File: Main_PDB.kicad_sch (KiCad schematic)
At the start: 126 parts, among them J1 Conn_01x02_MountingPin, J10 Conn_01x04_MountingPin, J11 Conn_01x08, J12 Conn_01x02_MountingPin, J2 Conn_01x02_MountingPin, J3 Conn_01x02_MountingPin, J4 Conn_01x02_MountingPin, J5 Conn_01x02_MountingPin, J6 Conn_01x01_MountingPin, J7 Conn_01x01_MountingPin, J8 Conn_01x02_MountingPin, Q1 PMOS, Q10 NMOS, Q11 NMOS, Q12 NMOS, Q13 NMOS, Q14 NMOS, Q15 NMOS, Q2 NPN, Q5 NMOS, Q7 NMOS, Q8 NMOS, Q9 NMOS, U1 LRM36015, U10 LM5148RGYR, U11 ACS758LCB-100U-PFF-T, U12 TPS48110AQDGXRQ1, U13 LM5148RGYR, U2 ACS758LCB-100U-PFF-T, U3 UCC27524AQDRQ1, U4 ACS758LCB-100U-PFF-T, U5 ACS758LCB-100U-PFF-T, U6 ACS758LCB-100U-PFF-T, U7 LTC4359HDCBPBF, U8 UCC27524AQDRQ1, U9 ACS758LCB-100U-PFF-T

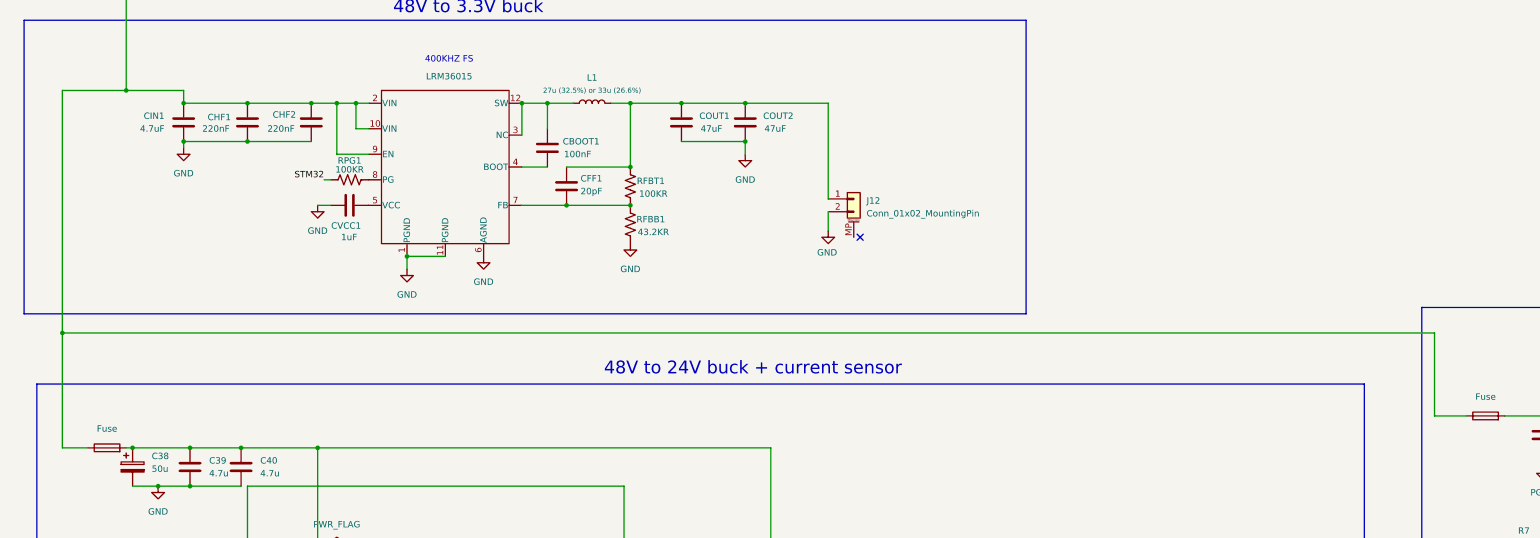
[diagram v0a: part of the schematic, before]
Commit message: Fixed 48V -> 6V buck power source
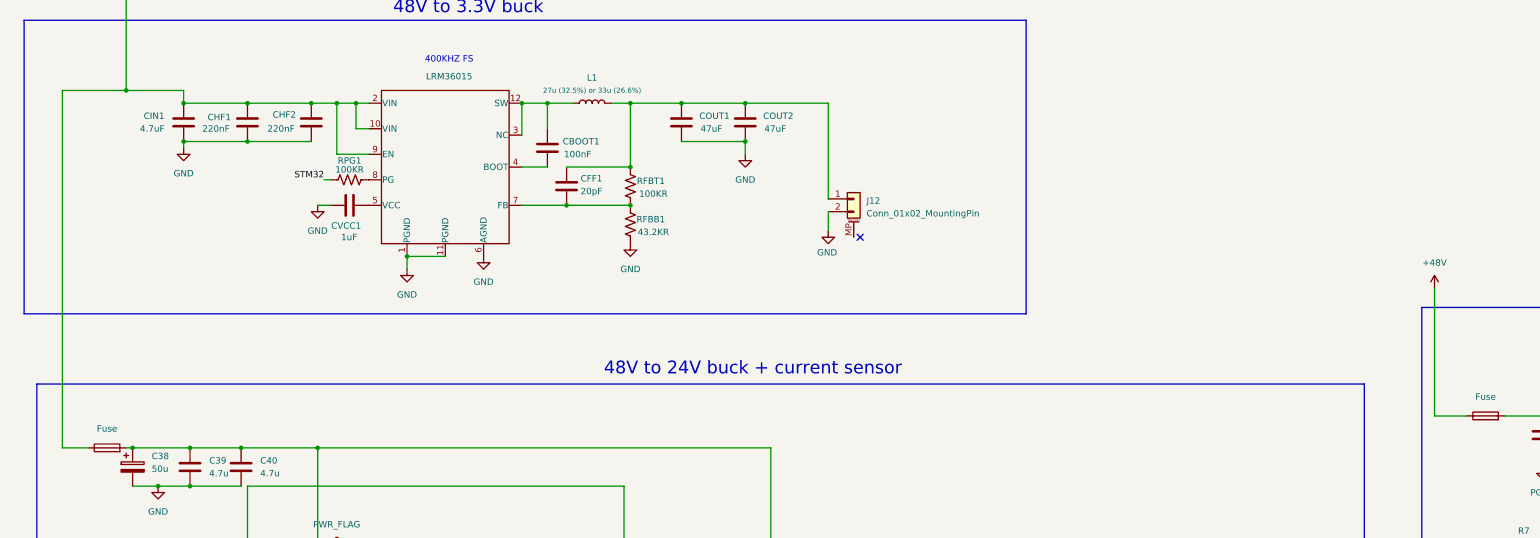
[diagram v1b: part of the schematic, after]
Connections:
- net +48V: now also F7.1
- net at CHF1.1, CHF2.1, CIN1.1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: no longer F7.1

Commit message: restructured actuator rails
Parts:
- removed C25: 47n, symbol Device:C
- removed C32, C51, C52: 100n, symbol Device:C
- removed D1, D2: ZYxxx, Diode_THT:D_DO-41_SOD81_P10.16mm_Horizontal, symbol Diode:ZYxxx
- removed J10: Conn_01x04_MountingPin, symbol Connector_Generic_MountingPin:Conn_01x04_MountingPin
- removed J11: Conn_01x08, symbol Connector_Generic_MountingPin:Conn_01x08_MountingPin
- removed J8: Conn_01x02_MountingPin, symbol Connector_Generic_MountingPin:Conn_01x02_MountingPin
- removed Q11, Q12, Q13, Q5: NMOS, symbol Simulation_SPICE:NMOS
- removed R13: 1k, symbol Device:R
- removed R4: R, symbol Device:R
- removed U3, U8: UCC27524AQDRQ1, UCC27524AQDRQ1:SOIC127P599X175-8N, symbol UCC27524AQDRQ1:UCC27524AQDRQ1
- removed U7: LTC4359HDCBPBF, LTC4359HDCBPBF:DFN-6_DCB, symbol LTC4359HDCBPBF:LTC4359HDCBPBF
- added C50, C53: 100n, symbol Device:C
- added J8: Conn_01x09_MountingPin, symbol Connector_Generic_MountingPin:Conn_01x09_MountingPin
- added J9: Conn_01x03_MountingPin, symbol Connector_Generic_MountingPin:Conn_01x03_MountingPin
- added U14: UCC27511DBVR, UCC27511DBVR:SOT95P280X145-6N, symbol UCC27511DBVR:UCC27511DBVR
- added U8: ACS758LCB-100U-PFF-T, ACS758LCB-100U-PFF-T:XDCR_ACS758LCB-100U-PFF-T, symbol ACS758LCB-100U-PFF-T:ACS758LCB-100U-PFF-T
- R2, R3: value R -> 4.7
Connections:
- net +48V: no longer F1.1, F2.1, F3.1, F4.1
- net +48V-B: now also C50.2, C53.1, J8.1 (Pin_1), U14.1 (VDD), U8.1 (VCC)
- net Com_cur: now also J8.8 (Pin_8)
- net GND: no longer R2.2, R3.2
- net GND1: now also C50.1, C53.2, J8.9 (Pin_9), U14.4 (GND), U14.5 (IN-), U8.2 (GND)
- net Main_curr: now also J8.7 (Pin_7)
- net at J6.1 (Pin_1): now also Q10.1 (D), U8.4 (IP+), U8.4_1 (IP+), U8.4_10 (IP+), U8.4_11 (IP+), U8.4_12 (IP+), U8.4_13 (IP+), U8.4_14 (IP+), U8.4_15 (IP+), U8.4_16 (IP+), U8.4_2 (IP+), U8.4_3 (IP+), U8.4_4 (IP+), U8.4_5 (IP+), U8.4_6 (IP+), U8.4_7 (IP+), U8.4_8 (IP+), U8.4_9 (IP+)
- net at U6.3 (VIOUT): now also J8.3 (Pin_3)
- net at C22.1, C23.1, C24.1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: no longer Q10.1 (D)
- net at R3.1: now also U14.3 (OUTL)
- net at U4.3 (VIOUT): now also J8.5 (Pin_5)
- net at R5.2: now also J9.3 (Pin_3)
- net at R2.1: now also U14.2 (OUTH)
- net at U2.3 (VIOUT): now also J8.6 (Pin_6)
- net at Q10.2 (G): now also R2.2, R3.2
- net at U5.3 (VIOUT): now also J8.4 (Pin_4)
- new net: F1.1, F2.1, F3.1, F4.1, U8.5 (IP-), U8.5_1 (IP-), U8.5_10 (IP-), U8.5_11 (IP-), U8.5_12 (IP-), U8.5_13 (IP-), U8.5_14 (IP-), U8.5_15 (IP-), U8.5_16 (IP-), U8.5_2 (IP-), U8.5_3 (IP-), U8.5_4 (IP-), U8.5_5 (IP-), U8.5_6 (IP-), U8.5_7 (IP-), U8.5_8 (IP-), U8.5_9 (IP-)
- new net Act_rail_curr: J8.2 (Pin_2), U8.3 (VIOUT)
- new net Back_curr_sing: J9.1 (Pin_1), U14.6 (IN+)
- no-connect marks 15 -> 10
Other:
- note removed: "Ideal diode"
- moved on the sheet: J6

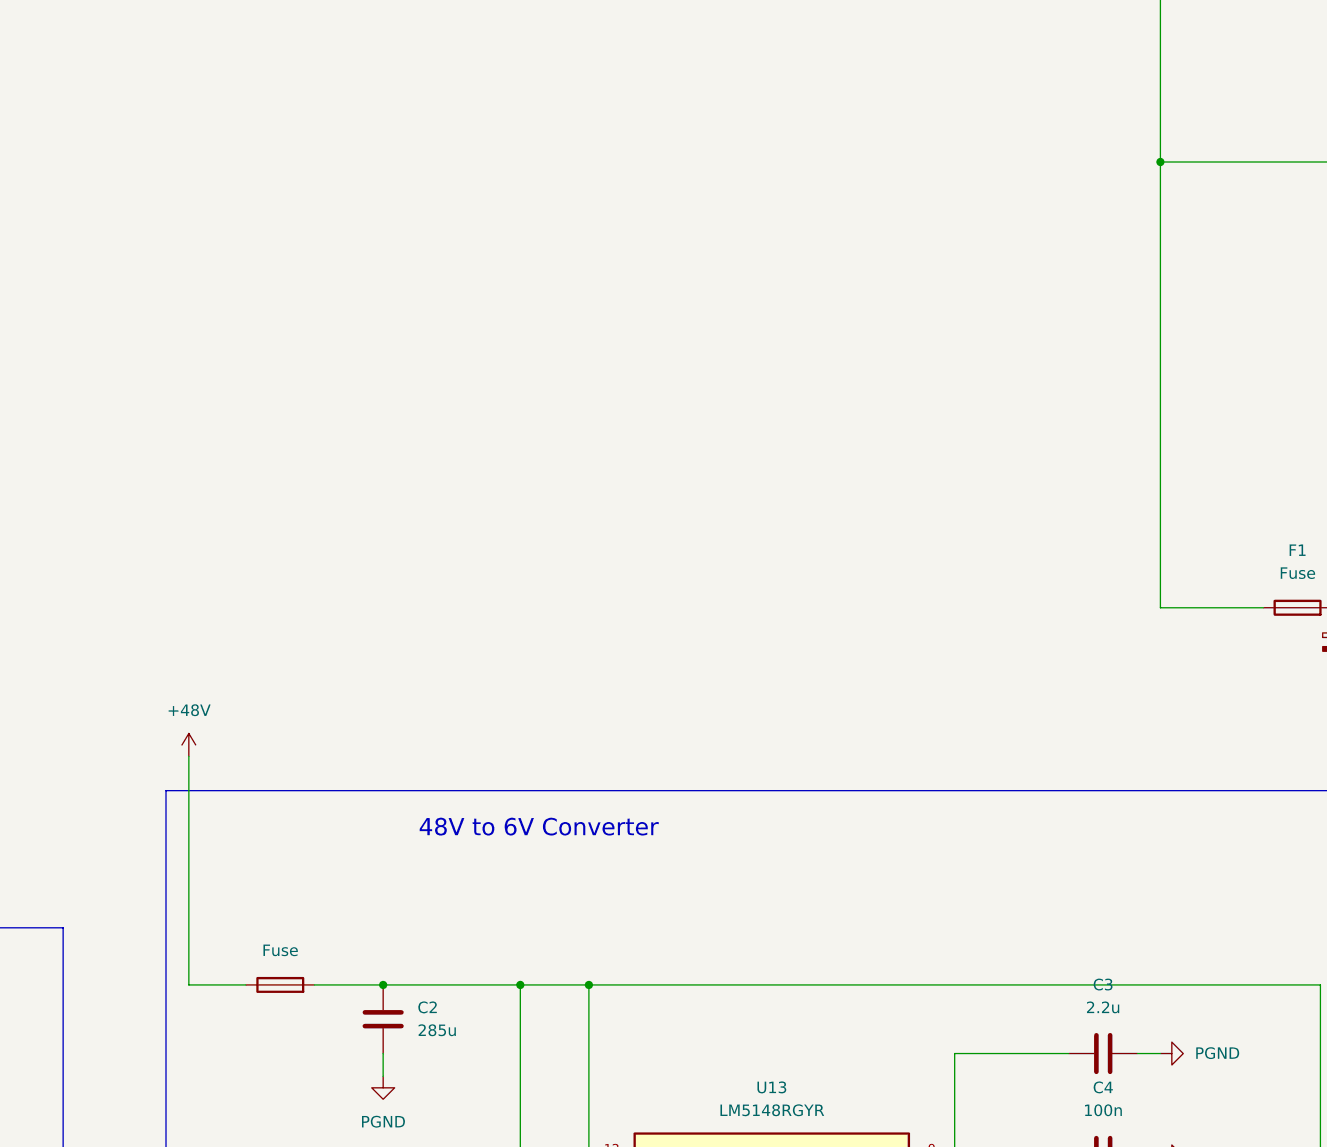
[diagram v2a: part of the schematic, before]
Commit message: 48->6 power conection update
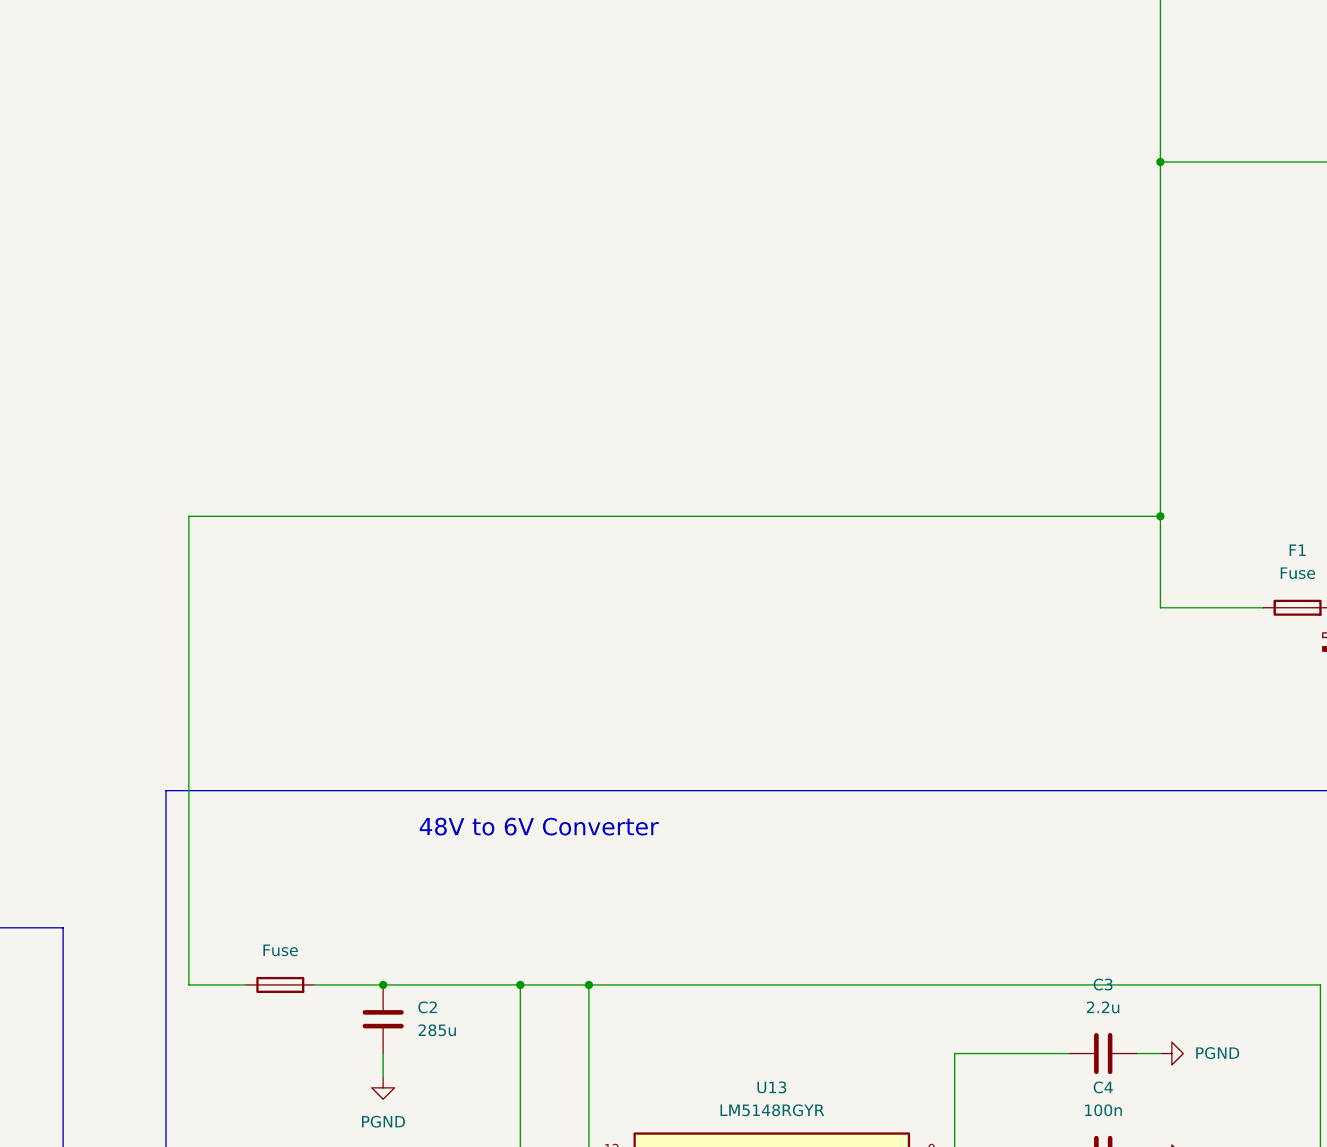
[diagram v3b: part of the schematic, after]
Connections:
- net +48V is gone; now on an unnamed net: F7.1
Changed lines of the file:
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@@
 	)
 	(junction
+		(at 405.13 210.82)
+		(diameter 0)
+		(color 0 0 0 0)
+	)
+	(junction
 		(at 445.77 171.45)
 		(diameter 0)
@@
 	(wire
 		(pts
-			(xy 405.13 220.98) (xy 405.13 171.45)
+			(xy 405.13 220.98) (xy 405.13 210.82)
 		)
 		(stroke
@@
 	(wire
 		(pts
-			(xy 297.18 237.49) (xy 297.18 262.89)
-		)
-		(stroke
-			(width 0)
-			(type default)
-		)
-	)
-	(wire
-		(pts
 			(xy 78.74 60.96) (xy 78.74 95.25)
 		)
@@
 	(wire
 		(pts
+			(xy 297.18 210.82) (xy 297.18 262.89)
+		)
+		(stroke
+			(width 0)
+			(type default)
+		)
+	)
+	(wire
+		(pts
 			(xy 485.14 176.53) (xy 485.14 189.23)
 		)
@@
 	(wire
 		(pts
+			(xy 405.13 210.82) (xy 405.13 171.45)
+		)
+		(stroke
+			(width 0)
+			(type default)
+		)
+	)
+	(wire
+		(pts
 			(xy 429.26 95.25) (xy 439.42 95.25)
 		)
@@
 	(wire
 		(pts
+			(xy 297.18 210.82) (xy 405.13 210.82)
+		)
+		(stroke
+			(width 0)
+			(type default)
+		)
+	)
+	(wire
+		(pts
 			(xy 119.38 31.75) (xy 119.38 44.45)
 		)
@@
 					(unit 1)
 				)
-			)
-		)
-	)
-	(symbol
-		(lib_id "power:+48V")
-		(at 297.18 237.49 0)
-		(unit 1)
-		(body_style 1)
-		(exclude_from_sim no)
-		(in_bom yes)
-		(on_board yes)
-		(in_pos_files yes)
-		(dnp no)
-		(fields_autoplaced yes)
-		(property "Reference" "#PWR060"
-			(at 297.18 241.3 0)
-			(hide yes)
-			(show_name no)
-			(do_not_autoplace no)
-			(effects
-				(font
-					(size 1.27 1.27)
-				)
-			)
-		)
-		(property "Value" "+48V"
-			(at 297.18 232.41 0)
-			(show_name no)
-			(do_not_autoplace no)
-			(effects
-				(font
-					(size 1.27 1.27)
-				)
-			)
-		)
-		(property "Footprint" ""
-			(at 297.18 237.49 0)
-			(hide yes)
-			(show_name no)
-			(do_not_autoplace no)
-			(effects
-				(font
-					(size 1.27 1.27)
-				)
-			)
-		)
-		(property "Datasheet" ""
-			(at 297.18 237.49 0)
-			(hide yes)
-			(show_name no)
-			(do_not_autoplace no)
-			(effects
-				(font
-					(size 1.27 1.27)
-				)
-			)
-		)
-		(property "Description" "Power symbol creates a global label with name \"+48V\""
-			(at 297.18 237.49 0)
-			(hide yes)
-			(show_name no)
-			(do_not_autoplace no)
-			(effects
-				(font
-					(size 1.27 1.27)
-				)
-			)
-		)
-		(pin "1"
-		)
-		(instances
-			(project "Main_PDB"
-				(path "/b0f96dc2-0eeb-4c9a-9b54-b0ba45b68ce7"
-					(reference "#PWR060")
-					(unit 1)
-				)

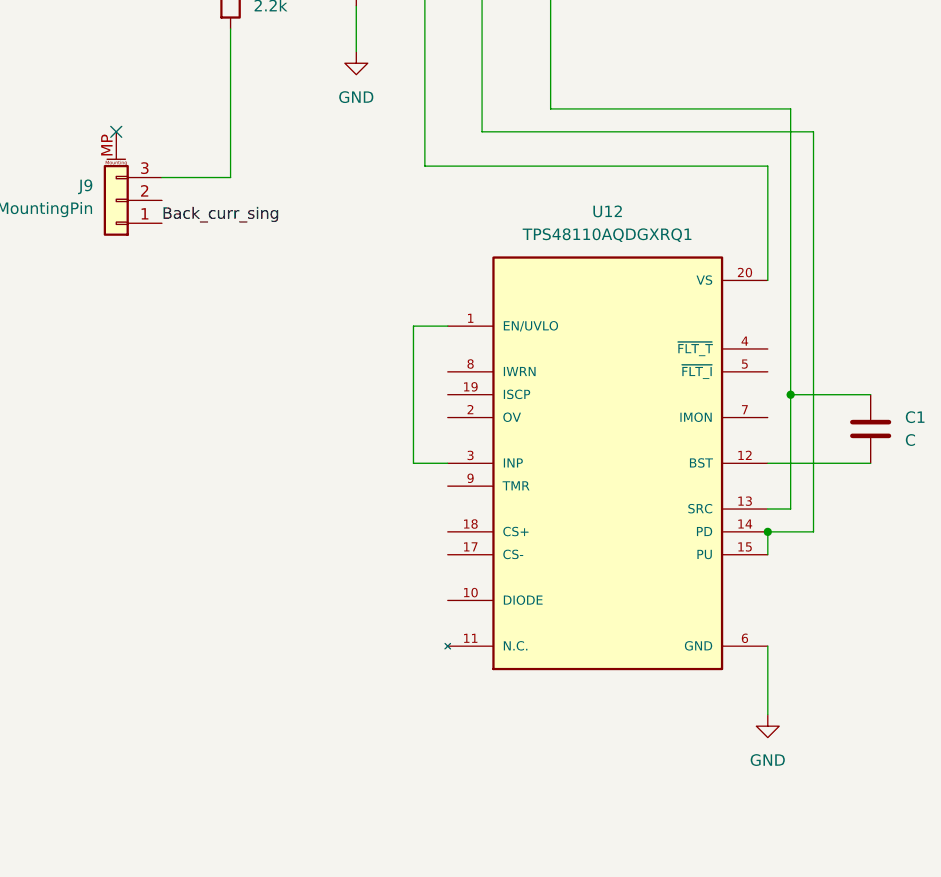
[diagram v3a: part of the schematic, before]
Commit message: Added precharge high side nmos controler
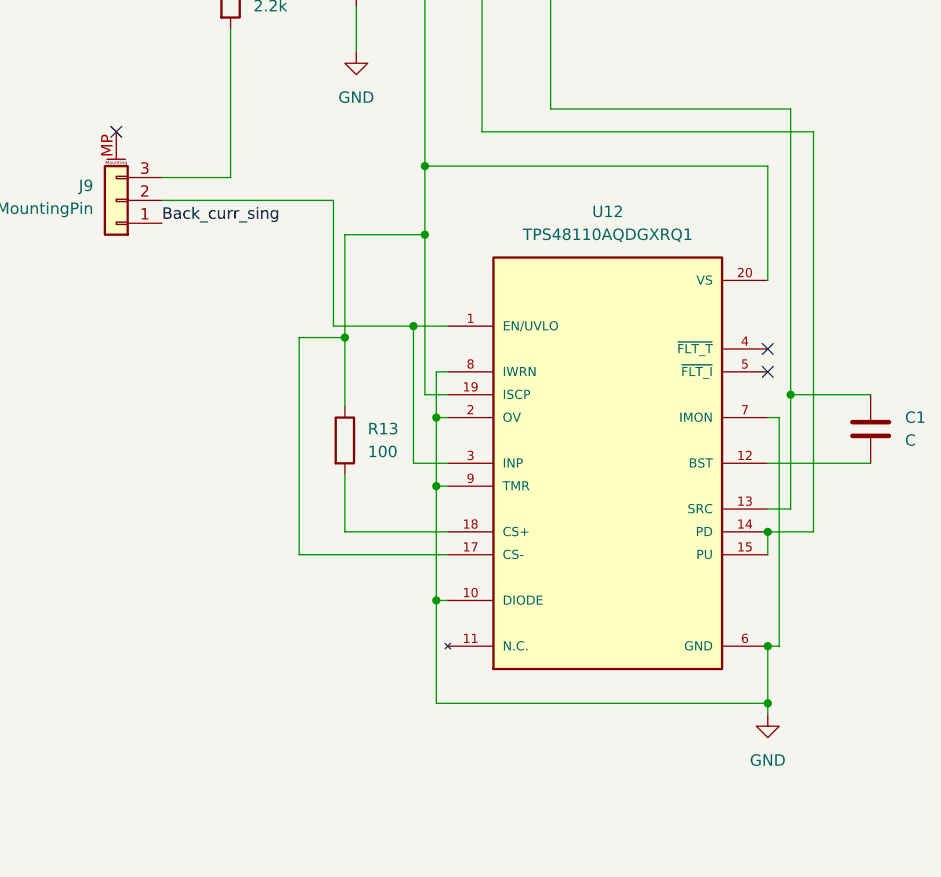
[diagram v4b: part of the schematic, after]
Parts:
- added R13: 100, symbol Device:R
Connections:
- net GND: now also U12.10 (DIODE), U12.2 (OV), U12.7 (IMON), U12.8 (IWRN), U12.9 (TMR)
- net at F5.2, Q1.1 (D), Q7.1 (D)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: now also U12.17 (CS-), U12.19 (ISCP), R13.1
- net at J9.2 (Pin_2): now also U12.1 (EN/UVLO), U12.3 (INP)
- net at U12.18 (CS+): now also R13.2
- no-connect marks 10 -> 12

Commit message: Changed current sensors to 3.3V
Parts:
- added J10: Conn_01x02_MountingPin, symbol Connector_Generic_MountingPin:Conn_01x02_MountingPin
- C48: value 400u -> 47u
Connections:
- net +48V-B: no longer C34.1, C35.1, C36.1, C37.1, C47.1, C50.2, C53.1, U11.1 (VCC), U14.1 (VDD), U2.1 (VCC), U4.1 (VCC), U5.1 (VCC), U6.1 (VCC), U8.1 (VCC)
- net AGND: now also J10.2 (Pin_2)
- net +3.3V: now reaches CFF1.1, COUT1.1, COUT2.1, J12.1 (Pin_1), L1.2, RFBT1.2
- net +3.3V: now also C34.1, C35.1, C36.1, C37.1, C47.1, C50.2, C53.1, U11.1 (VCC), U14.1 (VDD), U2.1 (VCC), U4.1 (VCC), U5.1 (VCC), U6.1 (VCC), U8.1 (VCC)
- net +6V: no longer names the net of C14.1, R10.2, R11.1, U13.21 (VOUT)
- net +6V: now also J10.1 (Pin_1)
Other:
- note added: "Actuator rails"
- note added: "Back current protection"
- note added: "Pre Charge"
- note added: "Pre charge driver"

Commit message: tvs diodes for overvoltage protection at the battery input
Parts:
- added D1, D2: TVS, symbol Device:D_Zener
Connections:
- net +48V-B: now also D1.1 (K), D2.1 (K)
- net GND: now also D1.2 (A), D2.2 (A)
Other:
- note added: "SMCJ58A TVS Diodes Input Overvoltage Protection"
- moved on the sheet: C13, C14, C2, C3, C38, C39, C4, C40, C41, C42, C43, C44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

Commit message: added TVS diodes for overvoltage protection for each actuator rail output and also the 24v and 6v rail outputs
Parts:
- added D3, D4, D5, D6, D7, D8: TVS, symbol Device:D_Zener
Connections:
- net GND: now also D3.2 (A), D4.2 (A), D5.2 (A), D6.2 (A), D7.2 (A), D8.2 (A)
- net at C14.1, J10.1 (Pin_1), R10.2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: now also D7.1 (K)
- net at J5.1 (Pin_1), U6.5 (IP-), U6.5_1 (IP-)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: now also D3.1 (K)
- net at J3.1 (Pin_1), U4.5 (IP-), U4.5_1 (IP-)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: now also D5.1 (K)
- net at J4.1 (Pin_1), U5.5 (IP-), U5.5_1 (IP-)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: now also D4.1 (K)
- net at J2.1 (Pin_1), U2.5 (IP-), U2.5_1 (IP-)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: now also D6.1 (K)
- net at C48.1, J1.1 (Pin_1), U11.5 (IP-)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: now also D8.1 (K)
